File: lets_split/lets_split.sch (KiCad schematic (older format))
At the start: 60 parts, among them J1 3PIN, J2 6PIN, J3 3PIN, SW1 SW_PUSH, SW10 SW_PUSH, SW11 SW_PUSH, SW12 SW_PUSH, SW13 SW_PUSH, SW14 SW_PUSH, SW15 SW_PUSH, SW16 SW_PUSH, SW17 SW_PUSH, SW18 SW_PUSH, SW19 SW_PUSH, SW2 SW_PUSH, SW20 SW_PUSH, SW21 SW_PUSH, SW22 SW_PUSH, SW23 SW_PUSH, SW24 SW_PUSH, SW3 SW_PUSH, SW4 SW_PUSH, SW5 SW_PUSH, SW6 SW_PUSH, SW7 SW_PUSH, SW8 SW_PUSH, SW9 SW_PUSH, U1 TEENSY2.0, U2 HOLE, U3 HOLE, U4 HOLE, U5 HOLE

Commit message: added universal switch and stuff
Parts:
- added J10, J11, J12, J4, J5, J6, J7, J8, J9: Conn_01x01, BishopKicadConsolidated:PIN_1, symbol Conn_01x01
- added SW25: SW_PUSH, Universal-Switch-Footprint:MX-ALPs-PG1350-FLIP-2U, symbol SW_PUSH
- SW1, SW10, SW11, SW12, SW13, SW14, SW15, SW16, SW17, SW18, SW19, SW2, SW20, SW21, SW22, SW23, SW24, SW3, SW4, SW5, SW6, SW7, SW8, SW9: footprint flipalps:MXALPS_FLIP -> Universal-Switch-Footprint:MX-ALPs-PG1350-FLIP
- W1: symbol TEST -> TEST-RESCUE-lets_split
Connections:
- wire segments 24 -> 25
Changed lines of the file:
@@
 EESchema Schematic File Version 2
+LIBS:lets_split-rescue
 LIBS:power
 LIBS:device
@@
 LIBS:contrib
 LIBS:valves
-LIBS:component
 LIBS:lets_split-cache
 EELAYER 25 0
@@
 F 0 "SW1" H 5600 2310 50  0000 C CNN
 F 1 "SW_PUSH" H 5450 2120 50  0000 C CNN
-F 2 "flipalps:MXALPS_FLIP" H 5450 2200 50  0001 C CNN
+F 2 "Universal-Switch-Footprint:MX-ALPs-PG1350-FLIP" H 5450 2200 50  0001 C CNN
 F 3 "" H 5450 2200 50  0000 C CNN
 	1    5450 2200
@@
 F 0 "SW5" H 6350 2310 50  0000 C CNN
 F 1 "SW_PUSH" H 6200 2120 50  0000 C CNN
-F 2 "flipalps:MXALPS_FLIP" H 6200 2200 50  0001 C CNN
+F 2 "Universal-Switch-Footprint:MX-ALPs-PG1350-FLIP" H 6200 2200 50  0001 C CNN
 F 3 "" H 6200 2200 50  0000 C CNN
 	1    6200 2200
@@
 F 0 "SW9" H 7050 2310 50  0000 C CNN
 F 1 "SW_PUSH" H 6900 2120 50  0000 C CNN
-F 2 "flipalps:MXALPS_FLIP" H 6900 2200 50  0001 C CNN
+F 2 "Universal-Switch-Footprint:MX-ALPs-PG1350-FLIP" H 6900 2200 50  0001 C CNN
 F 3 "" H 6900 2200 50  0000 C CNN
 	1    6900 2200
@@
 F 0 "SW13" H 7800 2310 50  0000 C CNN
 F 1 "SW_PUSH" H 7650 2120 50  0000 C CNN
-F 2 "flipalps:MXALPS_FLIP" H 7650 2200 50  0001 C CNN
+F 2 "Universal-Switch-Footprint:MX-ALPs-PG1350-FLIP" H 7650 2200 50  0001 C CNN
 F 3 "" H 7650 2200 50  0000 C CNN
 	1    7650 2200
@@
 F 0 "SW17" H 8550 2310 50  0000 C CNN
 F 1 "SW_PUSH" H 8400 2120 50  0000 C CNN
-F 2 "flipalps:MXALPS_FLIP" H 8400 2200 50  0001 C CNN
+F 2 "Universal-Switch-Footprint:MX-ALPs-PG1350-FLIP" H 8400 2200 50  0001 C CNN
 F 3 "" H 8400 2200 50  0000 C CNN
 	1    8400 2200
@@
 F 0 "SW21" H 9300 2310 50  0000 C CNN
 F 1 "SW_PUSH" H 9150 2120 50  0000 C CNN
-F 2 "flipalps:MXALPS_FLIP" H 9150 2200 50  0001 C CNN
+F 2 "Universal-Switch-Footprint:MX-ALPs-PG1350-FLIP" H 9150 2200 50  0001 C CNN
 F 3 "" H 9150 2200 50  0000 C CNN
 	1    9150 2200
@@
 F 0 "SW2" H 5600 2810 50  0000 C CNN
 F 1 "SW_PUSH" H 5450 2620 50  0000 C CNN
-F 2 "flipalps:MXALPS_FLIP" H 5450 2700 50  0001 C CNN
+F 2 "Universal-Switch-Footprint:MX-ALPs-PG1350-FLIP" H 5450 2700 50  0001 C CNN
 F 3 "" H 5450 2700 50  0000 C CNN
 	1    5450 2700
@@
 F 0 "SW6" H 6350 2810 50  0000 C CNN
 F 1 "SW_PUSH" H 6200 2620 50  0000 C CNN
-F 2 "flipalps:MXALPS_FLIP" H 6200 2700 50  0001 C CNN
+F 2 "Universal-Switch-Footprint:MX-ALPs-PG1350-FLIP" H 6200 2700 50  0001 C CNN
 F 3 "" H 6200 2700 50  0000 C CNN
 	1    6200 2700
@@
 F 0 "SW10" H 7050 2810 50  0000 C CNN
 F 1 "SW_PUSH" H 6900 2620 50  0000 C CNN
-F 2 "flipalps:MXALPS_FLIP" H 6900 2700 50  0001 C CNN
+F 2 "Universal-Switch-Footprint:MX-ALPs-PG1350-FLIP" H 6900 2700 50  0001 C CNN
 F 3 "" H 6900 2700 50  0000 C CNN
 	1    6900 2700
@@
 F 0 "SW14" H 7800 2810 50  0000 C CNN
 F 1 "SW_PUSH" H 7650 2620 50  0000 C CNN
-F 2 "flipalps:MXALPS_FLIP" H 7650 2700 50  0001 C CNN
+F 2 "Universal-Switch-Footprint:MX-ALPs-PG1350-FLIP" H 7650 2700 50  0001 C CNN
 F 3 "" H 7650 2700 50  0000 C CNN
 	1    7650 2700
@@
 F 0 "SW18" H 8550 2810 50  0000 C CNN
 F 1 "SW_PUSH" H 8400 2620 50  0000 C CNN
-F 2 "flipalps:MXALPS_FLIP" H 8400 2700 50  0001 C CNN
+F 2 "Universal-Switch-Footprint:MX-ALPs-PG1350-FLIP" H 8400 2700 50  0001 C CNN
 F 3 "" H 8400 2700 50  0000 C CNN
 	1    8400 2700
@@
 F 0 "SW22" H 9300 2810 50  0000 C CNN
 F 1 "SW_PUSH" H 9150 2620 50  0000 C CNN
-F 2 "flipalps:MXALPS_FLIP" H 9150 2700 50  0001 C CNN
+F 2 "Universal-Switch-Footprint:MX-ALPs-PG1350-FLIP" H 9150 2700 50  0001 C CNN
 F 3 "" H 9150 2700 50  0000 C CNN
 	1    9150 2700
@@
 F 0 "SW3" H 5600 3310 50  0000 C CNN
 F 1 "SW_PUSH" H 5450 3120 50  0000 C CNN
-F 2 "flipalps:MXALPS_FLIP" H 5450 3200 50  0001 C CNN
+F 2 "Universal-Switch-Footprint:MX-ALPs-PG1350-FLIP" H 5450 3200 50  0001 C CNN
 F 3 "" H 5450 3200 50  0000 C CNN
 	1    5450 3200
@@
 F 0 "SW7" H 6350 3310 50  0000 C CNN
 F 1 "SW_PUSH" H 6200 3120 50  0000 C CNN
-F 2 "flipalps:MXALPS_FLIP" H 6200 3200 50  0001 C CNN
+F 2 "Universal-Switch-Footprint:MX-ALPs-PG1350-FLIP" H 6200 3200 50  0001 C CNN
 F 3 "" H 6200 3200 50  0000 C CNN
 	1    6200 3200
@@
 F 0 "SW11" H 7050 3310 50  0000 C CNN
 F 1 "SW_PUSH" H 6900 3120 50  0000 C CNN
-F 2 "flipalps:MXALPS_FLIP" H 6900 3200 50  0001 C CNN
+F 2 "Universal-Switch-Footprint:MX-ALPs-PG1350-FLIP" H 6900 3200 50  0001 C CNN
 F 3 "" H 6900 3200 50  0000 C CNN
 	1    6900 3200
@@
 F 0 "SW15" H 7800 3310 50  0000 C CNN
 F 1 "SW_PUSH" H 7650 3120 50  0000 C CNN
-F 2 "flipalps:MXALPS_FLIP" H 7650 3200 50  0001 C CNN
+F 2 "Universal-Switch-Footprint:MX-ALPs-PG1350-FLIP" H 7650 3200 50  0001 C CNN
 F 3 "" H 7650 3200 50  0000 C CNN
 	1    7650 3200
@@
 F 0 "SW19" H 8550 3310 50  0000 C CNN
 F 1 "SW_PUSH" H 8400 3120 50  0000 C CNN
-F 2 "flipalps:MXALPS_FLIP" H 8400 3200 50  0001 C CNN
+F 2 "Universal-Switch-Footprint:MX-ALPs-PG1350-FLIP" H 8400 3200 50  0001 C CNN
 F 3 "" H 8400 3200 50  0000 C CNN
 	1    8400 3200
@@
 F 0 "SW23" H 9300 3310 50  0000 C CNN
 F 1 "SW_PUSH" H 9150 3120 50  0000 C CNN
-F 2 "flipalps:MXALPS_FLIP" H 9150 3200 50  0001 C CNN
+F 2 "Universal-Switch-Footprint:MX-ALPs-PG1350-FLIP" H 9150 3200 50  0001 C CNN
 F 3 "" H 9150 3200 50  0000 C CNN
 	1    9150 3200
@@
 F 0 "SW4" H 5600 3810 50  0000 C CNN
 F 1 "SW_PUSH" H 5450 3620 50  0000 C CNN
-F 2 "flipalps:MXALPS_FLIP" H 5450 3700 50  0001 C CNN
+F 2 "Universal-Switch-Footprint:MX-ALPs-PG1350-FLIP" H 5450 3700 50  0001 C CNN
 F 3 "" H 5450 3700 50  0000 C CNN
 	1    5450 3700
@@
 F 0 "SW8" H 6350 3810 50  0000 C CNN
 F 1 "SW_PUSH" H 6200 3620 50  0000 C CNN
-F 2 "flipalps:MXALPS_FLIP" H 6200 3700 50  0001 C CNN
+F 2 "Universal-Switch-Footprint:MX-ALPs-PG1350-FLIP" H 6200 3700 50  0001 C CNN
 F 3 "" H 6200 3700 50  0000 C CNN
 	1    6200 3700
@@
 F 0 "SW12" H 7050 3810 50  0000 C CNN
 F 1 "SW_PUSH" H 6900 3620 50  0000 C CNN
-F 2 "flipalps:MXALPS_FLIP" H 6900 3700 50  0001 C CNN
+F 2 "Universal-Switch-Footprint:MX-ALPs-PG1350-FLIP" H 6900 3700 50  0001 C CNN
 F 3 "" H 6900 3700 50  0000 C CNN
 	1    6900 3700
@@
 F 0 "SW16" H 7800 3810 50  0000 C CNN
 F 1 "SW_PUSH" H 7650 3620 50  0000 C CNN
-F 2 "flipalps:MXALPS_FLIP" H 7650 3700 50  0001 C CNN
+F 2 "Universal-Switch-Footprint:MX-ALPs-PG1350-FLIP" H 7650 3700 50  0001 C CNN
 F 3 "" H 7650 3700 50  0000 C CNN
 	1    7650 3700
@@
 F 0 "SW20" H 8550 3810 50  0000 C CNN
 F 1 "SW_PUSH" H 8400 3620 50  0000 C CNN
-F 2 "flipalps:MXALPS_FLIP" H 8400 3700 50  0001 C CNN
+F 2 "Universal-Switch-Footprint:MX-ALPs-PG1350-FLIP" H 8400 3700 50  0001 C CNN
 F 3 "" H 8400 3700 50  0000 C CNN
 	1    8400 3700
@@
 F 0 "SW24" H 9300 3810 50  0000 C CNN
 F 1 "SW_PUSH" H 9150 3620 50  0000 C CNN
-F 2 "flipalps:MXALPS_FLIP" H 9150 3700 50  0001 C CNN
+F 2 "Universal-Switch-Footprint:MX-ALPs-PG1350-FLIP" H 9150 3700 50  0001 C CNN
 F 3 "" H 9150 3700 50  0000 C CNN
 	1    9150 3700
@@
 xtradata
 $Comp
-L TEST W1
+L TEST-RESCUE-lets_split W1
 U 1 1 57D52188
 P 4400 900
@@
 	1    0    0    -1
 $EndComp
+$Comp
+L Conn_01x01 J4
+U 1 1 5B0F6BF0
+P 2800 1750
+F 0 "J4" H 2800 1850 50  0000 C CNN
+F 1 "Conn_01x01" H 2800 1650 50  0000 C CNN
+F 2 "BishopKicadConsolidated:PIN_1" H 2800 1750 50  0001 C CNN
+F 3 "" H 2800 1750 50  0001 C CNN
+	1    2800 1750
+	1    0    0    -1
+$EndComp
+$Comp
+L Conn_01x01 J5
+U 1 1 5B0F6D30
+P 2800 1950
+F 0 "J5" H 2800 2050 50  0000 C CNN
+F 1 "Conn_01x01" H 2800 1850 50  0000 C CNN
+F 2 "BishopKicadConsolidated:PIN_1" H 2800 1950 50  0001 C CNN
+F 3 "" H 2800 1950 50  0001 C CNN
+	1    2800 1950
+	1    0    0    -1
+$EndComp
+$Comp
+L Conn_01x01 J6
+U 1 1 5B0F6E1A
+P 2800 2250
+F 0 "J6" H 2800 2350 50  0000 C CNN
+F 1 "Conn_01x01" H 2800 2150 50  0000 C CNN
+F 2 "BishopKicadConsolidated:PIN_1" H 2800 2250 50  0001 C CNN
+F 3 "" H 2800 2250 50  0001 C CNN
+	1    2800 2250
+	1    0    0    -1
+$EndComp
+$Comp
+L Conn_01x01 J7
+U 1 1 5B0F6FC4
+P 2800 2350
+F 0 "J7" H 2800 2450 50  0000 C CNN
+F 1 "Conn_01x01" H 2800 2250 50  0000 C CNN
+F 2 "BishopKicadConsolidated:PIN_1" H 2800 2350 50  0001 C CNN
+F 3 "" H 2800 2350 50  0001 C CNN
+	1    2800 2350
+	1    0    0    -1
+$EndComp
+$Comp
+L Conn_01x01 J8
+U 1 1 5B0F75A0
+P 2800 3150
+F 0 "J8" H 2800 3250 50  0000 C CNN
+F 1 "Conn_01x01" H 2800 3050 50  0000 C CNN
+F 2 "BishopKicadConsolidated:PIN_1" H 2800 3150 50  0001 C CNN
+F 3 "" H 2800 3150 50  0001 C CNN
+	1    2800 3150
+	1    0    0    -1
+$EndComp
+$Comp
+L Conn_01x01 J9
+U 1 1 5B0F769F
+P 2800 3250
+F 0 "J9" H 2800 3350 50  0000 C CNN
+F 1 "Conn_01x01" H 2800 3150 50  0000 C CNN
+F 2 "BishopKicadConsolidated:PIN_1" H 2800 3250 50  0001 C CNN
+F 3 "" H 2800 3250 50  0001 C CNN
+	1    2800 3250
+	1    0    0    -1
+$EndComp
+$Comp
+L Conn_01x01 J10
+U 1 1 5B0F777F
+P 2800 3600
+F 0 "J10" H 2800 3700 50  0000 C CNN
+F 1 "Conn_01x01" H 2800 3500 50  0000 C CNN
+F 2 "BishopKicadConsolidated:PIN_1" H 2800 3600 50  0001 C CNN
+F 3 "" H 2800 3600 50  0001 C CNN
+	1    2800 3600
+	1    0    0    -1
+$EndComp
+$Comp
+L Conn_01x01 J11
+U 1 1 5B0F7870
+P 2800 3750
+F 0 "J11" H 2800 3850 50  0000 C CNN
+F 1 "Conn_01x01" H 2800 3650 50  0000 C CNN
+F 2 "BishopKicadConsolidated:PIN_1" H 2800 3750 50  0001 C CNN
+F 3 "" H 2800 3750 50  0001 C CNN
+	1    2800 3750
+	1    0    0    -1
+$EndComp
+$Comp
+L Conn_01x01 J12
+U 1 1 5B0F7B30
+P 2800 4250
+F 0 "J12" H 2800 4350 50  0000 C CNN
+F 1 "Conn_01x01" H 2800 4150 50  0000 C CNN
+F 2 "BishopKicadConsolidated:PIN_1" H 2800 4250 50  0001 C CNN
+F 3 "" H 2800 4250 50  0001 C CNN
+	1    2800 4250
+	1    0    0    -1
+$EndComp
+$Comp
+L SW_PUSH SW25
+U 1 1 5B0F8518
+P 9150 3600
+F 0 "SW25" H 9300 3710 50  0000 C CNN
+F 1 "SW_PUSH" H 9150 3520 50  0000 C CNN
+F 2 "Universal-Switch-Footprint:MX-ALPs-PG1350-FLIP-2U" H 9150 3600 50  0001 C CNN
+F 3 "" H 9150 3600 50  0000 C CNN
+	1    9150 3600
+	1    0    0    -1
+$EndComp
+Connection ~ 8850 3600
+Wire Wire Line
+	9450 3600 9450 3700
 $EndSCHEMATC

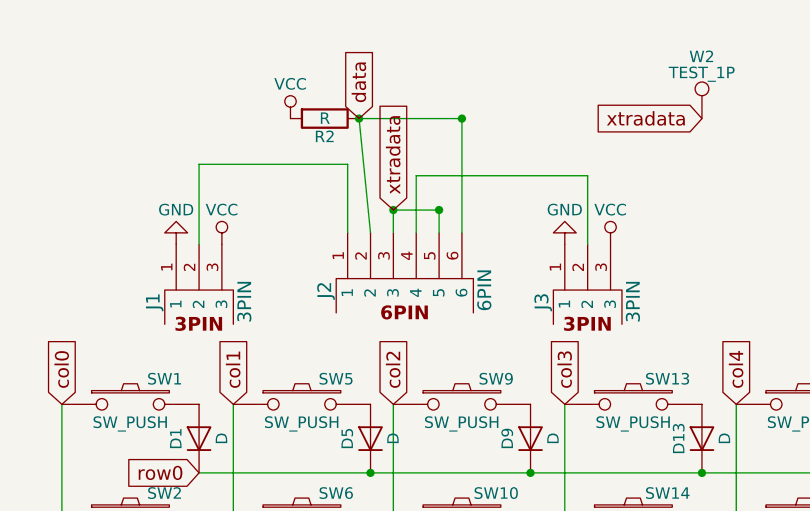
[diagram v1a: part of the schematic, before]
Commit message: changed 3.5mm jack
updated 3.5mm jack to use the PJ320E
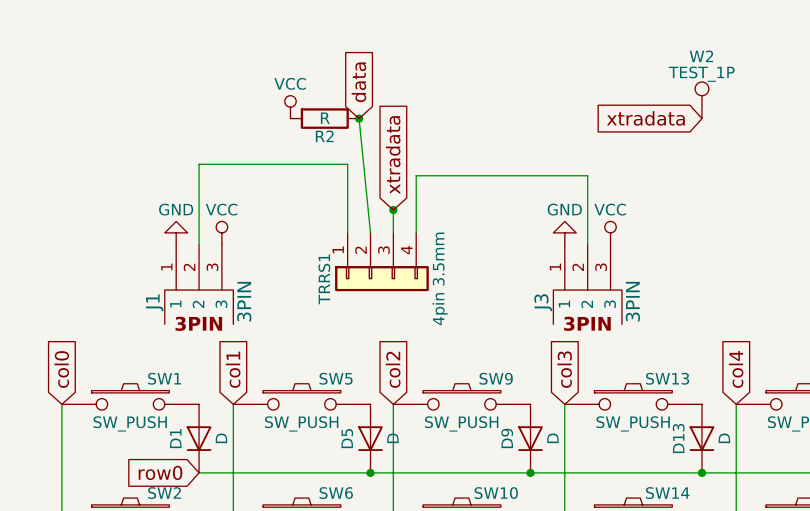
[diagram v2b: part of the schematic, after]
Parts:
- removed J2: 6PIN, footprint:4pin35mmAudio, symbol 6PIN
- added TRRS1: 4pin 3.5mm, BishopKicadConsolidated:PJ320E_3.5mm_Jack_flip, symbol Conn_01x04
- SW25: footprint Universal-Switch-Footprint:MX-ALPs-PG1350-FLIP-2U -> Universal-Switch-Footprint:MX-ALPs-PG1350-FLIP
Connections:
- net data: now also TRRS1.2 (Pin_2)
- net xtradata: now also TRRS1.3 (Pin_3)
- net at J1.2: now also TRRS1.1 (Pin_1)
- net at J3.2: now also TRRS1.4 (Pin_4)
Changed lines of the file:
@@
-$EndComp
-$Comp
-L 6PIN J2
-U 1 1 57D49FBD
-P 6650 1650
-F 0 "J2" H 6600 2000 60  0000 C CNN
-F 1 "6PIN" H 6600 1300 60  0000 C CNN
-F 2 "footprint:4pin35mmAudio" H 6650 1650 60  0001 C CNN
-F 3 "" H 6650 1650 60  0000 C CNN
-	1    6650 1650
-	0    -1   -1   0
 $EndComp
 $Comp
@@
 Wire Wire Line
 	6450 950  6500 1450
-Wire Wire Line
-	6450 950  6900 950
-Wire Wire Line
-	6900 950  6900 1450
-Connection ~ 6900 950
 Connection ~ 6450 950
 Wire Wire Line
-	6800 1450 6800 1350
-Wire Wire Line
-	6800 1350 6600 1350
-Wire Wire Line
 	6600 1350 6600 1450
-Connection ~ 6800 1350
 Connection ~ 6600 1350
 Text GLabel 6600 1350 1    60   Input ~ 0
@@
 F 0 "SW25" H 9300 3710 50  0000 C CNN
 F 1 "SW_PUSH" H 9150 3520 50  0000 C CNN
-F 2 "Universal-Switch-Footprint:MX-ALPs-PG1350-FLIP-2U" H 9150 3600 50  0001 C CNN
+F 2 "Universal-Switch-Footprint:MX-ALPs-PG1350-FLIP" H 9150 3600 50  0001 C CNN
 F 3 "" H 9150 3600 50  0000 C CNN
 	1    9150 3600
@@
 Wire Wire Line
 	9450 3600 9450 3700
+$Comp
+L Conn_01x04 TRRS1
+U 1 1 5B1217E6
+P 6500 1650
+F 0 "TRRS1" H 6500 1850 50  0000 C CNN
+F 1 "4pin 3.5mm" H 6500 1350 50  0000 C CNN
+F 2 "BishopKicadConsolidated:PJ320E_3.5mm_Jack_flip" H 6500 1650 50  0001 C CNN
+F 3 "" H 6500 1650 50  0001 C CNN
+	1    6500 1650
+	0    -1   1    0
+$EndComp
 $EndSCHEMATC
